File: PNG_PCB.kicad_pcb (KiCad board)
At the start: 2 copper layers, 59.2 x 68.2 mm, 109 parts, among them J1 connector, J10 connector, J11 connector, J12 connector, J13 connector, J14 connector, J15 connector, J16 connector, J17 connector, J18 connector, J19 connector, J2 connector, J20 connector, J21 connector, J22 connector, J23 connector, J24 connector, J25 connector, J26 connector, J27 connector, J28 connector, J29 connector, J3 connector, J30 connector, J4 connector, J5 connector, J6 connector, J7 connector, J8 connector, J9 connector, U1 Teensy4.1, U2 Mux, U3 MCP6004, U4 Mux, U5 Mux, U6 MCP6004, U7 Mux, U8 Mux, U9 MCP6004

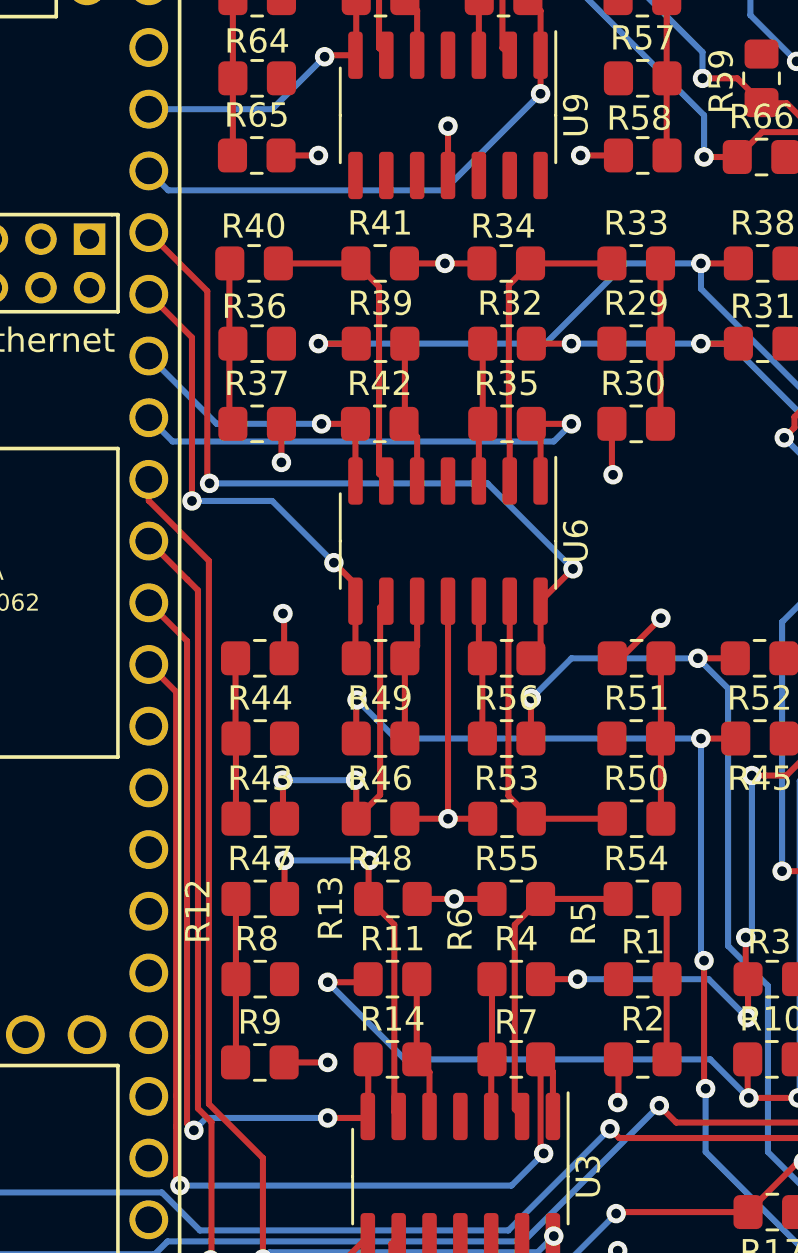
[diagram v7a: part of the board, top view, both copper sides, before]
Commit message: moved some vias for better power plane
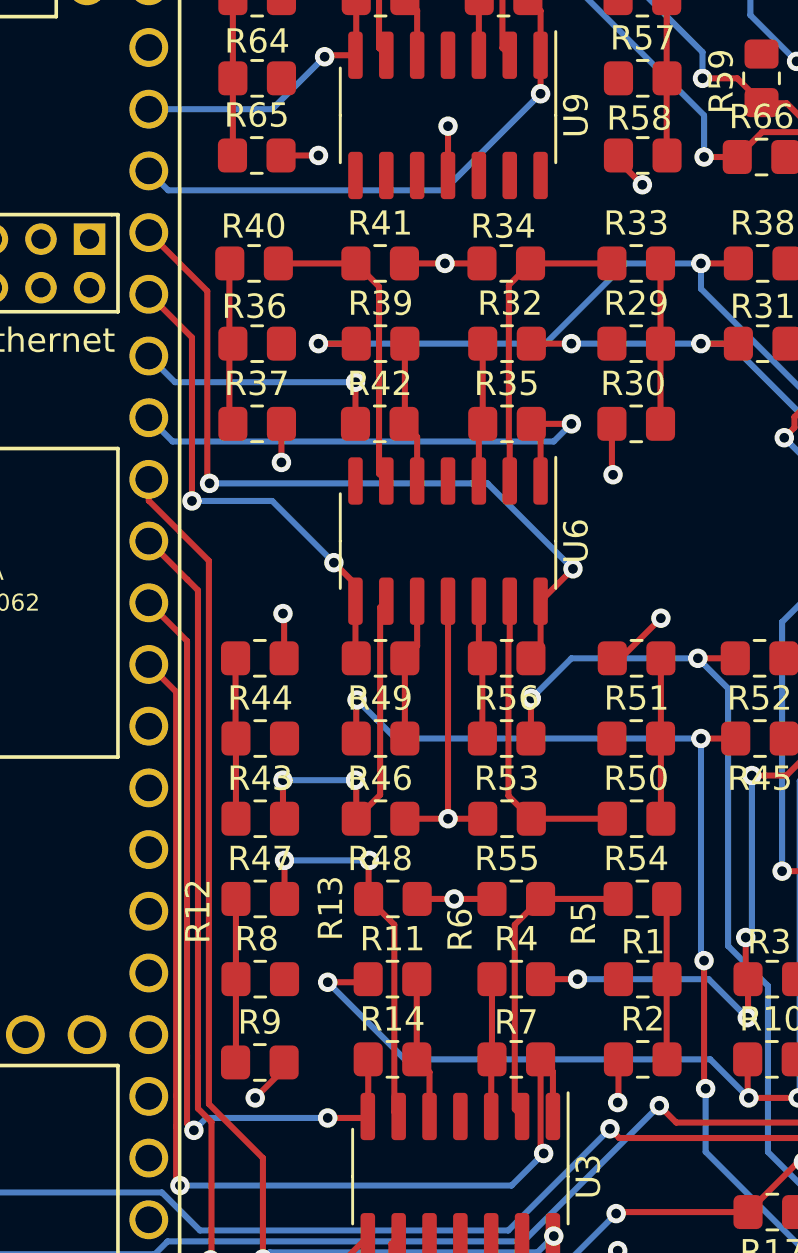
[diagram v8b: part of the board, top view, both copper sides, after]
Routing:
- net /ADC_IN_5: track 12.0 -> 10.7 mm
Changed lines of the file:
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@@
     (thickness 1.6)
     (drawings 1)
-    (tracks 734)
+    (tracks 735)
     (zones 0)
     (modules 109)
@@
   (via (at 161.925 56.261) (size 0.8) (drill 0.4) (layers F.Cu B.Cu) (net 1))
   (segment (start 160.385 56.261) (end 161.925 56.261) (width 0.25) (layer F.Cu) (net 1))
-  (via (at 172.72 56.261) (size 0.8) (drill 0.4) (layers F.Cu B.Cu) (net 1))
-  (segment (start 174.276 56.261) (end 172.72 56.261) (width 0.25) (layer F.Cu) (net 1))
   (via (at 156.972 46.482) (size 0.8) (drill 0.4) (layers F.Cu B.Cu) (net 1))
   (segment (start 158.401 46.482) (end 156.972 46.482) (width 0.25) (layer F.Cu) (net 1))
@@
   (segment (start 167.767 100.773) (end 167.767 109.601) (width 0.25) (layer F.Cu) (net 1))
   (segment (start 174.276 103.092) (end 174.244 103.124) (width 0.25) (layer F.Cu) (net 1))
-  (via (at 162.306 93.599) (size 0.8) (drill 0.4) (layers F.Cu B.Cu) (net 1))
-  (segment (start 160.512 93.599) (end 162.306 93.599) (width 0.25) (layer F.Cu) (net 1))
   (via (at 174.244 95.25) (size 0.8) (drill 0.4) (layers F.Cu B.Cu) (net 1))
   (segment (start 174.276 95.218) (end 174.244 95.25) (width 0.25) (layer F.Cu) (net 1))
@@
   (segment (start 160.528 103.124) (end 162.297186 103.124) (width 0.25) (layer F.Cu) (net 1))
   (via (at 162.304993 103.131807) (size 0.8) (drill 0.4) (layers F.Cu B.Cu) (net 1))
+  (via (at 175.26 57.4675) (size 0.8) (drill 0.4) (layers F.Cu B.Cu) (net 1))
+  (segment (start 174.276 56.4835) (end 175.26 57.4675) (width 0.25) (layer F.Cu) (net 1))
+  (segment (start 174.276 56.261) (end 174.276 56.4835) (width 0.25) (layer F.Cu) (net 1))
+  (via (at 159.3215 95.0595) (size 0.8) (drill 0.4) (layers F.Cu B.Cu) (net 1))
+  (segment (start 160.512 93.869) (end 159.3215 95.0595) (width 0.25) (layer F.Cu) (net 1))
+  (segment (start 160.512 93.599) (end 160.512 93.869) (width 0.25) (layer F.Cu) (net 1))
   (via (at 186.71651 78.223202) (size 0.8) (drill 0.4) (layers F.Cu B.Cu) (net 2))
   (segment (start 184.342 77.724) (end 186.055 77.724) (width 0.25) (layer F.Cu) (net 2))
@@
   (segment (start 177.673 60.706) (end 177.673 61.748561) (width 0.25) (layer B.Cu) (net 37))
   (segment (start 185.64201 71.548711) (end 184.770155 72.420566) (width 0.25) (layer F.Cu) (net 37))
-  (segment (start 163.449 67.31) (end 163.449 69.661) (width 0.25) (layer F.Cu) (net 38))
-  (via (at 162.052 67.31) (size 0.8) (drill 0.4) (layers F.Cu B.Cu) (net 38))
-  (segment (start 163.449 67.31) (end 162.052 67.31) (width 0.25) (layer F.Cu) (net 38))
-  (segment (start 157.734 67.31) (end 154.94 64.516) (width 0.25) (layer B.Cu) (net 38))
-  (segment (start 162.052 67.31) (end 157.734 67.31) (width 0.25) (layer B.Cu) (net 38))
+  (via (at 163.449 65.5955) (size 0.8) (drill 0.4) (layers F.Cu B.Cu) (net 38))
+  (segment (start 163.449 67.31) (end 163.449 65.5955) (width 0.25) (layer F.Cu) (net 38))
+  (segment (start 156.0195 65.5955) (end 154.94 64.516) (width 0.25) (layer B.Cu) (net 38))
+  (segment (start 163.449 65.5955) (end 156.0195 65.5955) (width 0.25) (layer B.Cu) (net 38))
   (via (at 185.780621 101.434459) (size 0.8) (drill 0.4) (layers F.Cu B.Cu) (net 39))
   (segment (start 184.493959 101.434459) (end 184.342 101.2825) (width 0.25) (layer F.Cu) (net 39))
